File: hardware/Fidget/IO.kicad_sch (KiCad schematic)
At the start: 8 parts

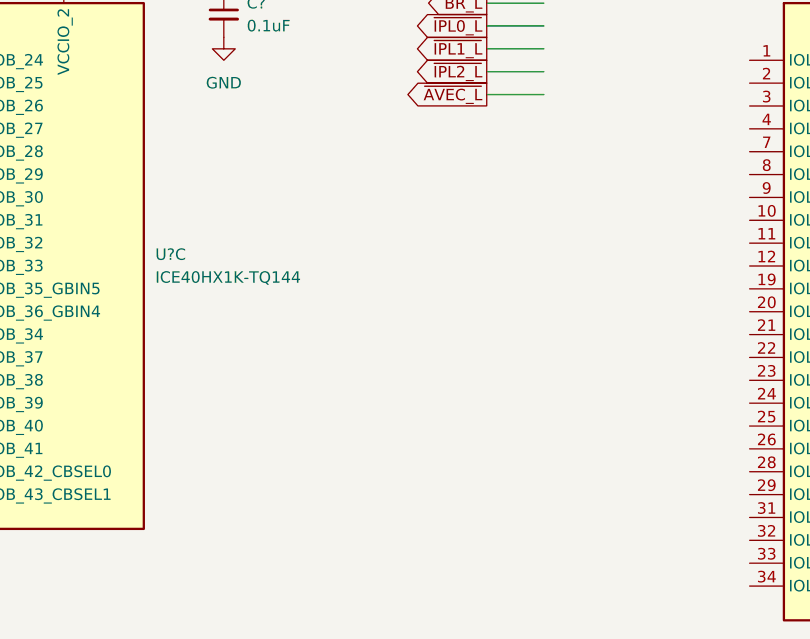
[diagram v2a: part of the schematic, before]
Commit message: Added address latches
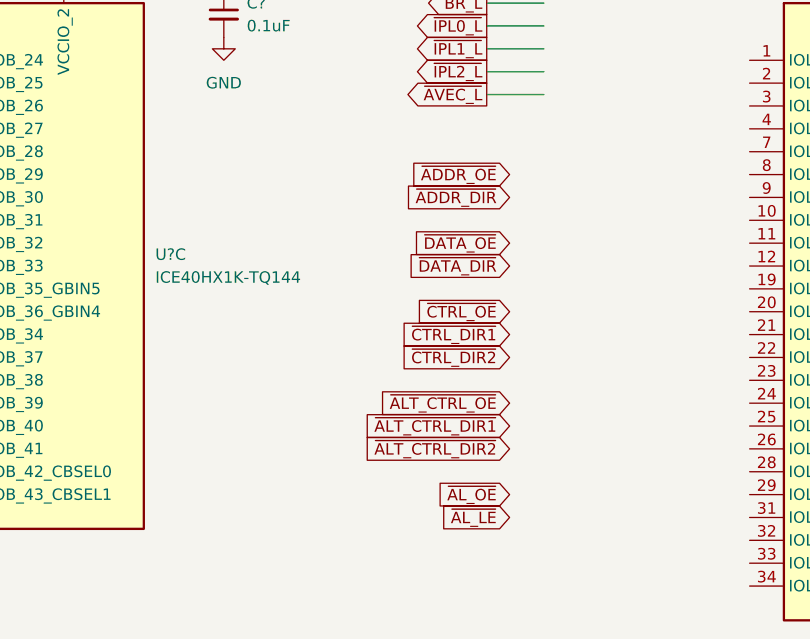
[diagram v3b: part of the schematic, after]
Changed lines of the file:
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@@
     (effects (font (size 1.27 1.27)) (justify left bottom))
   )
+  (global_label "~{DATA_DIR}" (shape input) (at 116.84 149.86 180) (fields_autoplaced)
+    (effects (font (size 1.27 1.27)) (justify right))
+    (property "Intersheet References" "${INTERSHEET_REFS}" (id 0) (at 105.8998 149.7806 0)
+      (effects (font (size 1.27 1.27)) (justify right) hide)
+    )
+  )
   (global_label "~{SCS}" (shape output) (at 49.53 142.24 180) (fields_autoplaced)
     (effects (font (size 1.27 1.27)) (justify right))
@@
     )
   )
+  (global_label "~{AL_OE}" (shape input) (at 116.84 175.26 180) (fields_autoplaced)
+    (effects (font (size 1.27 1.27)) (justify right))
+    (property "Intersheet References" "${INTERSHEET_REFS}" (id 0) (at 108.8631 175.1806 0)
+      (effects (font (size 1.27 1.27)) (justify right) hide)
+    )
+  )
   (global_label "~{AS_L}" (shape input) (at 114.3 45.72 180) (fields_autoplaced)
     (effects (font (size 1.27 1.27)) (justify right))
@@
     )
   )
+  (global_label "~{CTRL_DIR1}" (shape input) (at 116.84 157.48 180) (fields_autoplaced)
+    (effects (font (size 1.27 1.27)) (justify right))
+    (property "Intersheet References" "${INTERSHEET_REFS}" (id 0) (at 104.5693 157.4006 0)
+      (effects (font (size 1.27 1.27)) (justify right) hide)
+    )
+  )
   (global_label "~{BR_L}" (shape output) (at 114.3 120.65 180) (fields_autoplaced)
     (effects (font (size 1.27 1.27)) (justify right))
@@
     )
   )
+  (global_label "~{DATA_OE}" (shape input) (at 116.84 147.32 180) (fields_autoplaced)
+    (effects (font (size 1.27 1.27)) (justify right))
+    (property "Intersheet References" "${INTERSHEET_REFS}" (id 0) (at 106.565 147.2406 0)
+      (effects (font (size 1.27 1.27)) (justify right) hide)
+    )
+  )
   (global_label "CLK_L" (shape input) (at 39.37 60.96 180) (fields_autoplaced)
     (effects (font (size 1.27 1.27)) (justify right))
@@
     )
   )
+  (global_label "~{ALT_CTRL_DIR2}" (shape input) (at 116.84 170.18 180) (fields_autoplaced)
+    (effects (font (size 1.27 1.27)) (justify right))
+    (property "Intersheet References" "${INTERSHEET_REFS}" (id 0) (at 100.5174 170.1006 0)
+      (effects (font (size 1.27 1.27)) (justify right) hide)
+    )
+  )
   (global_label "~{SF_WP}" (shape output) (at 49.53 144.78 180) (fields_autoplaced)
     (effects (font (size 1.27 1.27)) (justify right))
@@
     )
   )
+  (global_label "~{CTRL_DIR2}" (shape input) (at 116.84 160.02 180) (fields_autoplaced)
+    (effects (font (size 1.27 1.27)) (justify right))
+    (property "Intersheet References" "${INTERSHEET_REFS}" (id 0) (at 104.5693 159.9406 0)
+      (effects (font (size 1.27 1.27)) (justify right) hide)
+    )
+  )
   (global_label "~{DSACK1_L}" (shape output) (at 115.57 74.93 180) (fields_autoplaced)
     (effects (font (size 1.27 1.27)) (justify right))
@@
     )
   )
+  (global_label "~{ALT_CTRL_DIR1}" (shape input) (at 116.84 167.64 180) (fields_autoplaced)
+    (effects (font (size 1.27 1.27)) (justify right))
+    (property "Intersheet References" "${INTERSHEET_REFS}" (id 0) (at 100.5174 167.5606 0)
+      (effects (font (size 1.27 1.27)) (justify right) hide)
+    )
+  )
   (global_label "USB_DP" (shape bidirectional) (at 41.91 129.54 180) (fields_autoplaced)
     (effects (font (size 1.27 1.27)) (justify right))
@@
     )
   )
+  (global_label "~{ADDR_DIR}" (shape input) (at 116.84 142.24 180) (fields_autoplaced)
+    (effects (font (size 1.27 1.27)) (justify right))
+    (property "Intersheet References" "${INTERSHEET_REFS}" (id 0) (at 105.4159 142.1606 0)
+      (effects (font (size 1.27 1.27)) (justify right) hide)
+    )
+  )
   (global_label "FC2_L" (shape input) (at 114.3 63.5 180) (fields_autoplaced)
     (effects (font (size 1.27 1.27)) (justify right))
@@
     )
   )
+  (global_label "~{AL_LE}" (shape input) (at 116.84 177.8 180) (fields_autoplaced)
+    (effects (font (size 1.27 1.27)) (justify right))
+    (property "Intersheet References" "${INTERSHEET_REFS}" (id 0) (at 109.1655 177.7206 0)
+      (effects (font (size 1.27 1.27)) (justify right) hide)
+    )
+  )
   (global_label "R{slash}~{W}_L" (shape input) (at 114.3 53.34 180) (fields_autoplaced)
     (effects (font (size 1.27 1.27)) (justify right))
@@
     )
   )
+  (global_label "~{ADDR_OE}" (shape input) (at 116.84 139.7 180) (fields_autoplaced)
+    (effects (font (size 1.27 1.27)) (justify right))
+    (property "Intersheet References" "${INTERSHEET_REFS}" (id 0) (at 106.0812 139.6206 0)
+      (effects (font (size 1.27 1.27)) (justify right) hide)
+    )
+  )
   (global_label "SIZ0_L" (shape input) (at 114.3 48.26 180) (fields_autoplaced)
     (effects (font (size 1.27 1.27)) (justify right))
@@
     )
   )
+  (global_label "~{CTRL_OE}" (shape input) (at 116.84 154.94 180) (fields_autoplaced)
+    (effects (font (size 1.27 1.27)) (justify right))
+    (property "Intersheet References" "${INTERSHEET_REFS}" (id 0) (at 106.444 154.8606 0)
+      (effects (font (size 1.27 1.27)) (justify right) hide)
+    )
+  )
   (global_label "~{RESET_L}" (shape bidirectional) (at 39.37 63.5 180) (fields_autoplaced)
     (effects (font (size 1.27 1.27)) (justify right))
@@
       (effects (font (size 1.27 1.27)) (justify right) hide)
     )
+  )
+  (global_label "~{ALT_CTRL_OE}" (shape input) (at 116.84 165.1 180) (fields_autoplaced)
+    (effects (font (size 1.27 1.27)) (justify right))
+    (property "Intersheet References" "${INTERSHEET_REFS}" (id 0) (at 102.3921 165.0206 0)
+      (effects (font (size 1.27 1.27)) (justify right) hide)
+    )

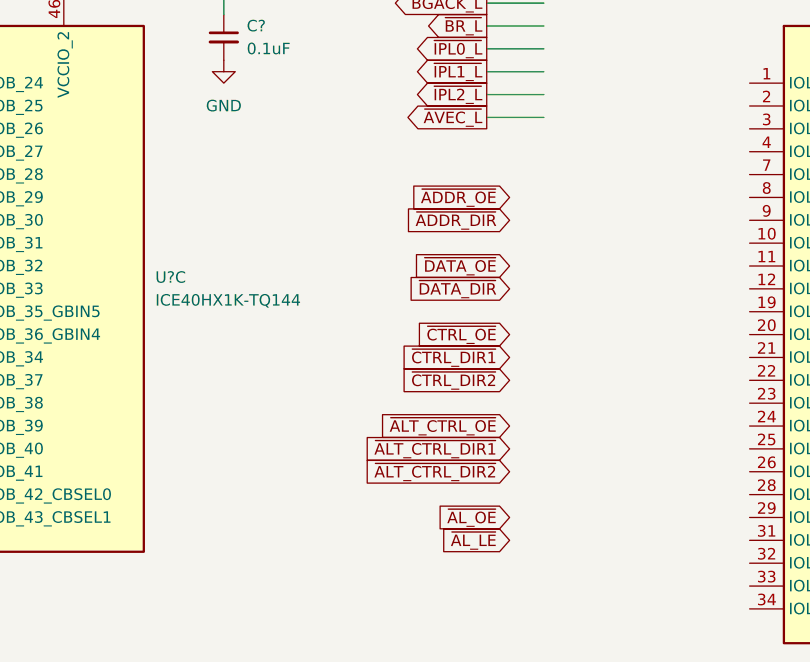
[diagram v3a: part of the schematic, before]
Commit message: Progress on sorting out the transceiver controls
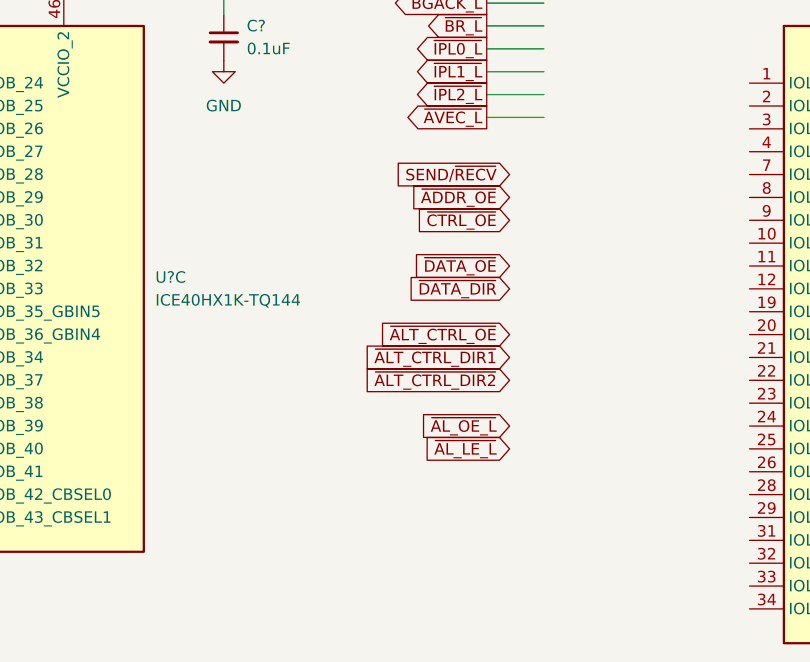
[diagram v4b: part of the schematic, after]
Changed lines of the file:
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@@
     )
   )
-  (global_label "~{AL_OE}" (shape input) (at 116.84 175.26 180) (fields_autoplaced)
-    (effects (font (size 1.27 1.27)) (justify right))
-    (property "Intersheet References" "${INTERSHEET_REFS}" (id 0) (at 108.8631 175.1806 0)
+  (global_label "~{AL_OE_L}" (shape input) (at 116.84 165.1 180) (fields_autoplaced)
+    (effects (font (size 1.27 1.27)) (justify right))
+    (property "Intersheet References" "${INTERSHEET_REFS}" (id 0) (at 106.8674 165.0206 0)
       (effects (font (size 1.27 1.27)) (justify right) hide)
     )
@@
     )
   )
-  (global_label "~{CTRL_DIR1}" (shape input) (at 116.84 157.48 180) (fields_autoplaced)
-    (effects (font (size 1.27 1.27)) (justify right))
-    (property "Intersheet References" "${INTERSHEET_REFS}" (id 0) (at 104.5693 157.4006 0)
-      (effects (font (size 1.27 1.27)) (justify right) hide)
-    )
-  )
   (global_label "~{BR_L}" (shape output) (at 114.3 120.65 180) (fields_autoplaced)
     (effects (font (size 1.27 1.27)) (justify right))
@@
     )
   )
-  (global_label "~{ALT_CTRL_DIR2}" (shape input) (at 116.84 170.18 180) (fields_autoplaced)
-    (effects (font (size 1.27 1.27)) (justify right))
-    (property "Intersheet References" "${INTERSHEET_REFS}" (id 0) (at 100.5174 170.1006 0)
+  (global_label "~{ALT_CTRL_DIR2}" (shape input) (at 116.84 160.02 180) (fields_autoplaced)
+    (effects (font (size 1.27 1.27)) (justify right))
+    (property "Intersheet References" "${INTERSHEET_REFS}" (id 0) (at 100.5174 159.9406 0)
       (effects (font (size 1.27 1.27)) (justify right) hide)
     )
@@
     )
   )
-  (global_label "~{CTRL_DIR2}" (shape input) (at 116.84 160.02 180) (fields_autoplaced)
-    (effects (font (size 1.27 1.27)) (justify right))
-    (property "Intersheet References" "${INTERSHEET_REFS}" (id 0) (at 104.5693 159.9406 0)
-      (effects (font (size 1.27 1.27)) (justify right) hide)
-    )
-  )
   (global_label "~{DSACK1_L}" (shape output) (at 115.57 74.93 180) (fields_autoplaced)
     (effects (font (size 1.27 1.27)) (justify right))
@@
     )
   )
-  (global_label "~{ALT_CTRL_DIR1}" (shape input) (at 116.84 167.64 180) (fields_autoplaced)
-    (effects (font (size 1.27 1.27)) (justify right))
-    (property "Intersheet References" "${INTERSHEET_REFS}" (id 0) (at 100.5174 167.5606 0)
+  (global_label "~{ALT_CTRL_DIR1}" (shape input) (at 116.84 157.48 180) (fields_autoplaced)
+    (effects (font (size 1.27 1.27)) (justify right))
+    (property "Intersheet References" "${INTERSHEET_REFS}" (id 0) (at 100.5174 157.4006 0)
       (effects (font (size 1.27 1.27)) (justify right) hide)
     )
@@
     )
   )
-  (global_label "~{ADDR_DIR}" (shape input) (at 116.84 142.24 180) (fields_autoplaced)
-    (effects (font (size 1.27 1.27)) (justify right))
-    (property "Intersheet References" "${INTERSHEET_REFS}" (id 0) (at 105.4159 142.1606 0)
-      (effects (font (size 1.27 1.27)) (justify right) hide)
-    )
-  )
   (global_label "FC2_L" (shape input) (at 114.3 63.5 180) (fields_autoplaced)
     (effects (font (size 1.27 1.27)) (justify right))
@@
     )
   )
-  (global_label "~{AL_LE}" (shape input) (at 116.84 177.8 180) (fields_autoplaced)
-    (effects (font (size 1.27 1.27)) (justify right))
-    (property "Intersheet References" "${INTERSHEET_REFS}" (id 0) (at 109.1655 177.7206 0)
+  (global_label "~{AL_LE_L}" (shape input) (at 116.84 167.64 180) (fields_autoplaced)
+    (effects (font (size 1.27 1.27)) (justify right))
+    (property "Intersheet References" "${INTERSHEET_REFS}" (id 0) (at 107.1698 167.5606 0)
       (effects (font (size 1.27 1.27)) (justify right) hide)
     )
@@
     )
   )
+  (global_label "SEND{slash}~{RECV}" (shape input) (at 116.84 137.16 180) (fields_autoplaced)
+    (effects (font (size 1.27 1.27)) (justify right))
+    (property "Intersheet References" "${INTERSHEET_REFS}" (id 0) (at 103.3598 137.0806 0)
+      (effects (font (size 1.27 1.27)) (justify right) hide)
+    )
+  )
   (global_label "~{HALT_L}" (shape output) (at 114.3 113.03 180) (fields_autoplaced)
     (effects (font (size 1.27 1.27)) (justify right))
@@
     )
   )
-  (global_label "~{CTRL_OE}" (shape input) (at 116.84 154.94 180) (fields_autoplaced)
-    (effects (font (size 1.27 1.27)) (justify right))
-    (property "Intersheet References" "${INTERSHEET_REFS}" (id 0) (at 106.444 154.8606 0)
+  (global_label "~{CTRL_OE}" (shape input) (at 116.84 142.24 180) (fields_autoplaced)
+    (effects (font (size 1.27 1.27)) (justify right))
+    (property "Intersheet References" "${INTERSHEET_REFS}" (id 0) (at 106.444 142.1606 0)
       (effects (font (size 1.27 1.27)) (justify right) hide)
     )
@@
     )
   )
-  (global_label "~{ALT_CTRL_OE}" (shape input) (at 116.84 165.1 180) (fields_autoplaced)
-    (effects (font (size 1.27 1.27)) (justify right))
-    (property "Intersheet References" "${INTERSHEET_REFS}" (id 0) (at 102.3921 165.0206 0)
-      (effects (font (size 1.27 1.27)) (justify right) hide)
-    )
+  (global_label "~{ALT_CTRL_OE}" (shape input) (at 116.84 154.94 180) (fields_autoplaced)
+    (effects (font (size 1.27 1.27)) (justify right))
+    (property "Intersheet References" "${INTERSHEET_REFS}" (id 0) (at 102.3921 154.8606 0)
+      (effects (font (size 1.27 1.27)) (justify right) hide)
+    )
